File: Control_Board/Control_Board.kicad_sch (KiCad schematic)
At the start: 56 parts, among them J1 DE9_Receptacle, J2 DE9_Receptacle, J3 Conn_01x04, J4 GPS_ANT, J5 Conn_01x02, SW2 SW_SPST, U1 STM32F446RCTx, U3 SN65HVD256D, U6 AP2204K-ADJ, U7 AP2204K-ADJ, U8 SN65HVD256D, U9 NEO-XM, Y3 8M, Y4 32.768k

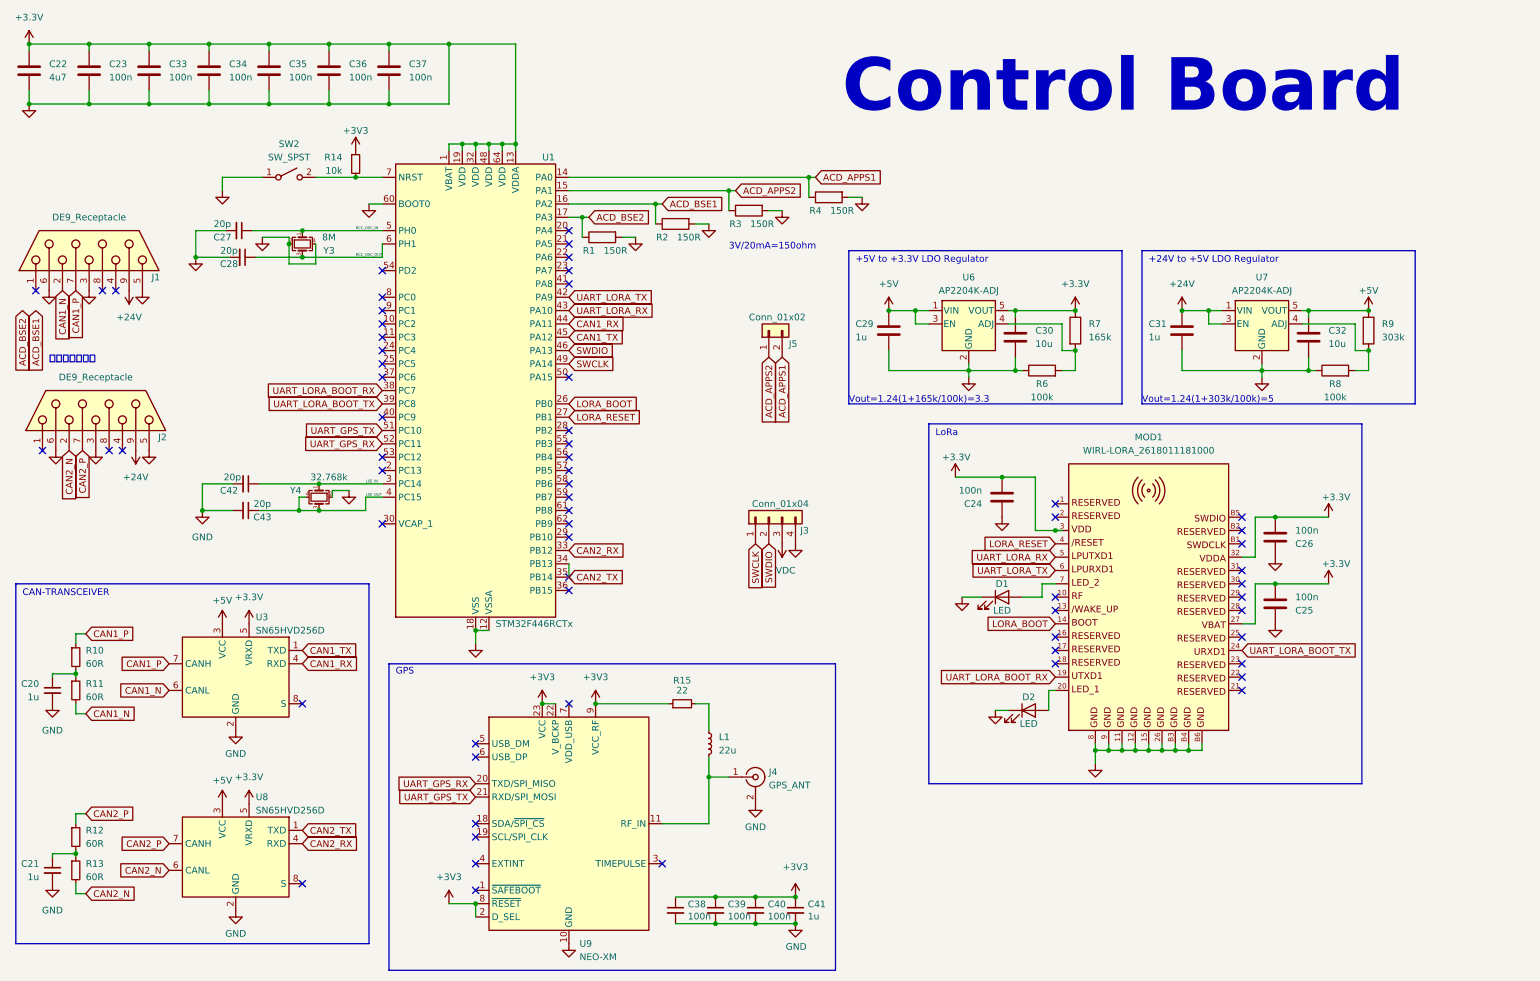
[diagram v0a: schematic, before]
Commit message: fix: power symbol and connector
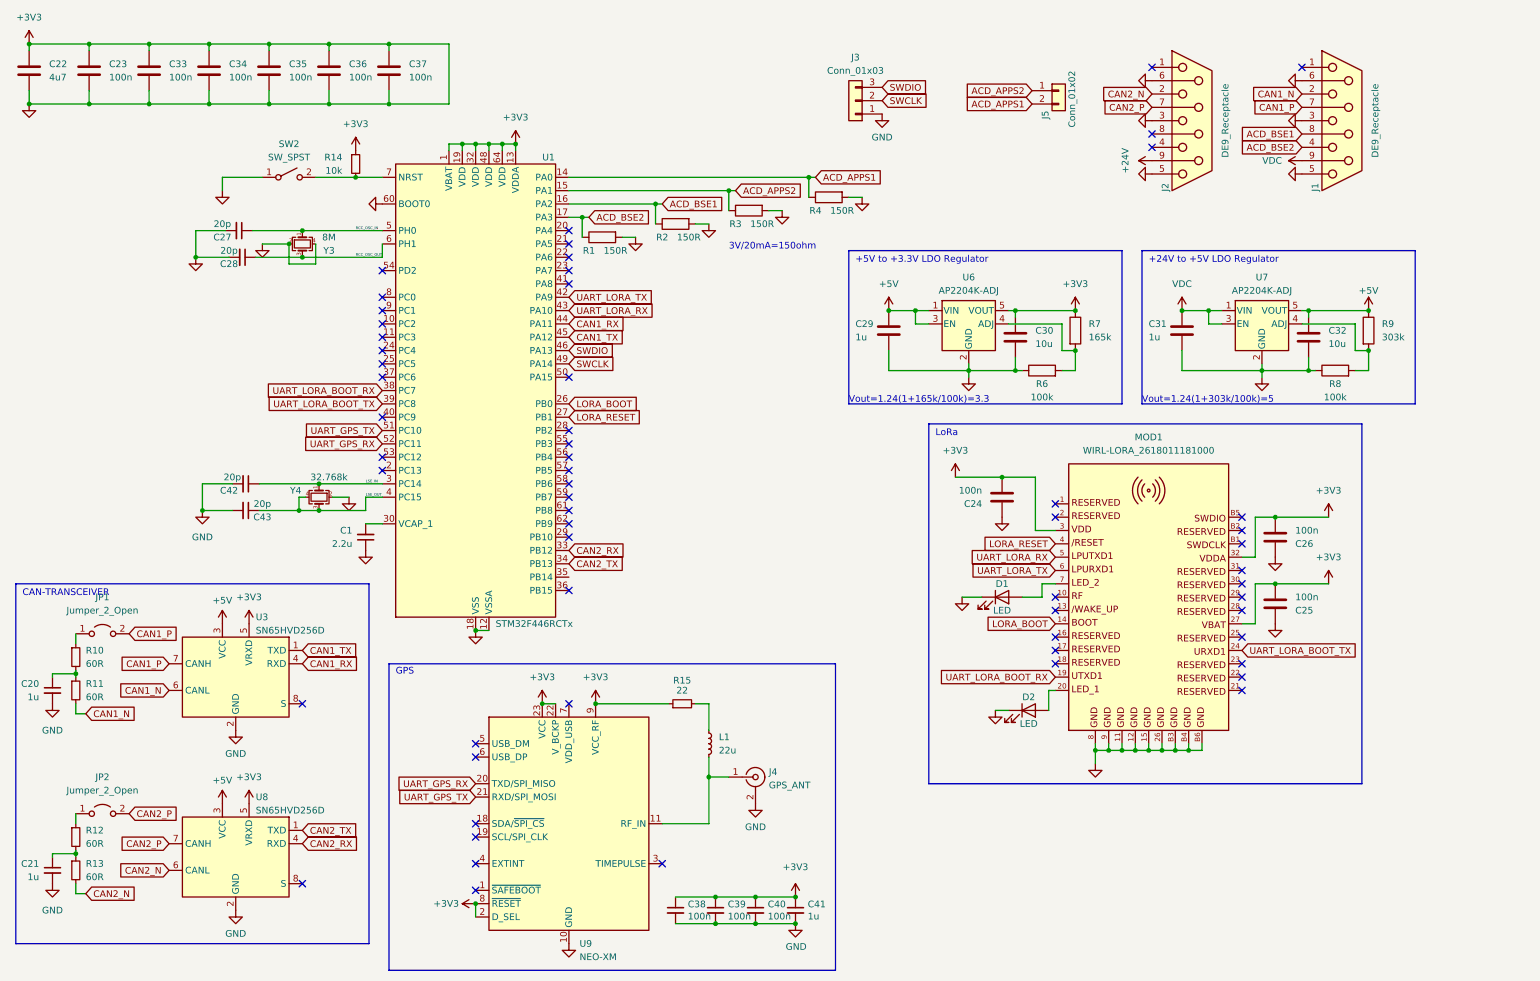
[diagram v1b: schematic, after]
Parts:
- removed J3: Conn_01x04, symbol Connector_Generic:Conn_01x04
- added C1: 2.2u, symbol Device:C_Small
- added J3: Conn_01x03, symbol Connector_Generic:Conn_01x03
- added JP1, JP2: Jumper_2_Open, symbol Jumper:Jumper_2_Open
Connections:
- net +3.3V is gone; now on net +3V3: C20.2, C21.2, C22.1, C22.2, C23.1, C23.2, C24.1, C24.2, C25.1, C25.2, C26.1, C26.2, C27.2, C28.2, C29.2, C30.1, C30.2, C31.2, C32.2, C33.1, C33.2, C34.1, C34.2, C35.1, C35.2, C36.1, C36.2, C37.1, C37.2, C38.2, C39.2, C40.2, C41.2, C42.2, C43.2, D1.1 (K), D2.1 (K), J1.3, J1.5, J1.6, J2.3, J2.5, J2.6, J4.2 (Ext), MOD1.11, MOD1.12, MOD1.15, MOD1.26, MOD1.27, MOD1.3, MOD1.32, MOD1.8, MOD1.9, MOD1.B3, MOD1.B4, MOD1.B6, R1.2, R2.2, R3.2, R4.2, R6.1, R7.1, R8.1, SW2.1 (A), U1.1 (VBAT), U1.12 (VSSA), U1.13 (VDDA), U1.18 (VSS), U1.19 (VDD), U1.31 (VSS), U1.32 (VDD), U1.47 (VSS), U1.48 (VDD), U1.60 (BOOT0), U1.63 (VSS), U1.64 (VDD), U3.2 (GND), U3.5 (VRXD), U6.2 (GND), U6.5 (VOUT), U7.2 (GND), U8.2 (GND), U8.5 (VRXD), U9.10 (GND), U9.12 (GND), U9.13 (GND), U9.24 (GND), Y3.2, Y3.4, Y4.2
- net +24V: no longer C31.1, J1.9, U7.1 (VIN), U7.3 (EN)
- net +3V3: now also C1.1, J3.1 (Pin_1)
- net ACD_BSE1: now also J1.8
- net ACD_BSE2: now also J1.4
- net CAN1_P: now also JP1.2 (B); no longer R10.1
- net CAN2_P: now also JP2.2 (B); no longer R12.1
- net CAN2_TX: no longer U1.35 (PB14)
- net SWCLK: now also J3.2 (Pin_2)
- net SWDIO: now also J3.3 (Pin_3)
- net VDC: now also C31.1, J1.9, U7.1 (VIN), U7.3 (EN)
- net at U1.30 (VCAP_1): now also C1.2
- new net: JP1.1 (A), R10.1
- new net: JP2.1 (A), R12.1
- no-connect marks 63 -> 59
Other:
- note removed: "Control Board"
- note removed: "還不確定要接哪"
- moved on the sheet: J1, J2, J5

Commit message: feat: implement schematic and select footprints
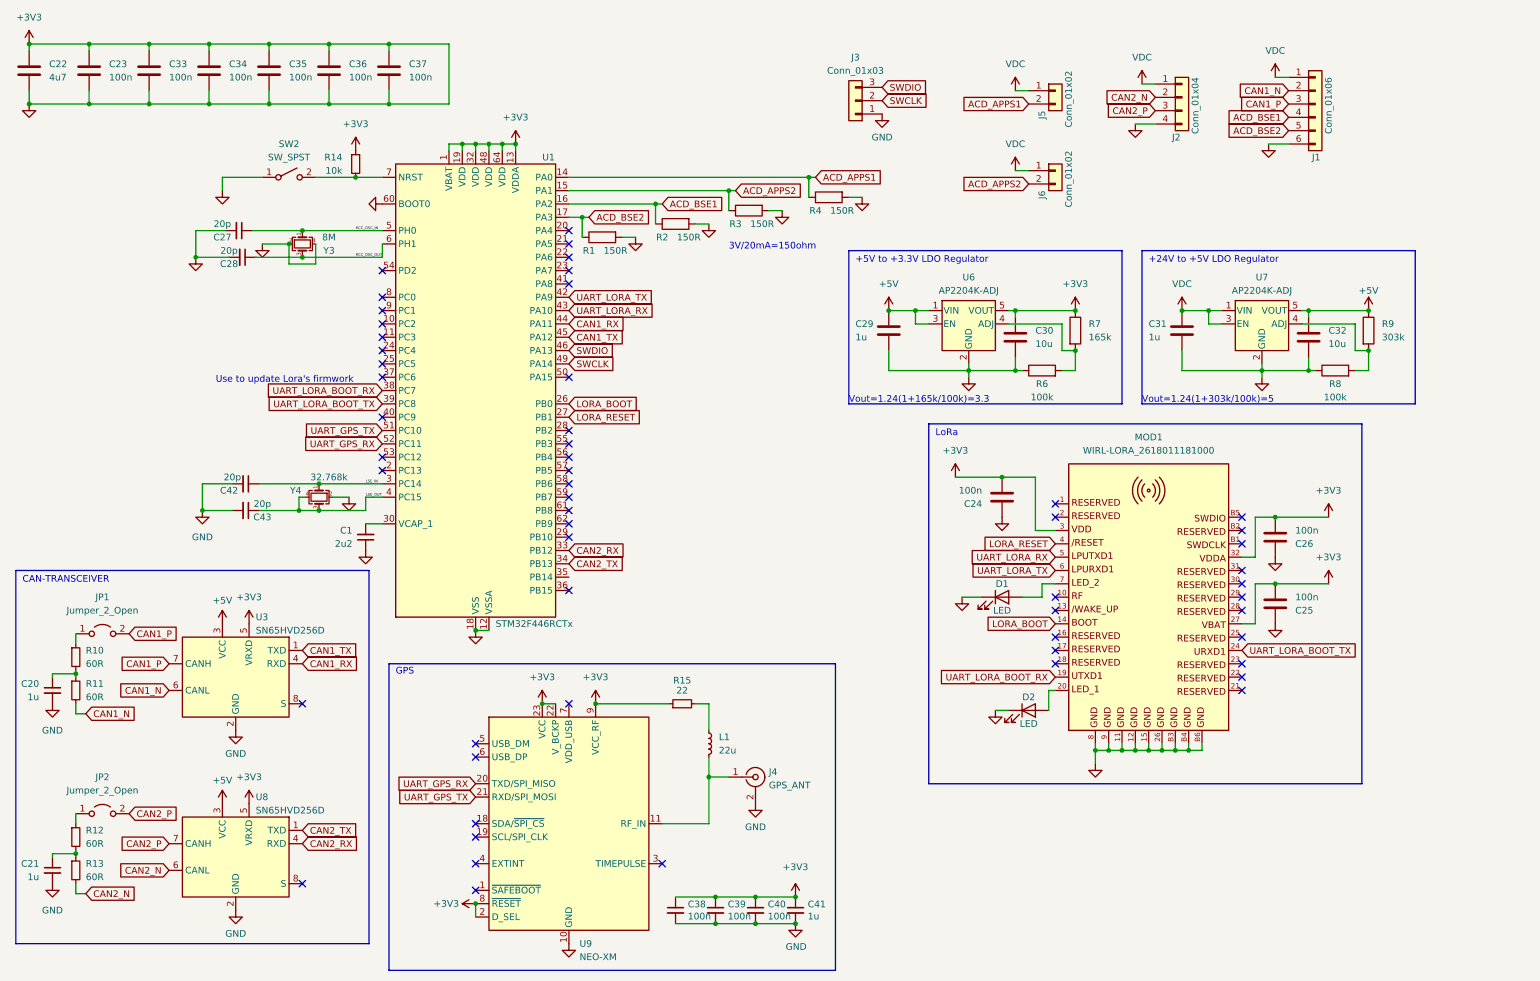
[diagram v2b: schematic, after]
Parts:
- removed J1, J2: DE9_Receptacle, symbol Connector:DE9_Receptacle
- added J1: Conn_01x06, Connector_JST:JST_XH_B6B-XH-A_1x06_P2.50mm_Vertical, symbol Connector_Generic:Conn_01x06
- added J2: Conn_01x04, Connector_JST:JST_XH_B4B-XH-A_1x04_P2.50mm_Vertical, symbol Connector_Generic:Conn_01x04
- added J6: Conn_01x02, Connector_JST:JST_XH_B2B-XH-A_1x02_P2.50mm_Vertical, symbol Connector_Generic:Conn_01x02
- C1: value 2.2u -> 2u2; footprint (none) -> Capacitor_SMD:C_0805_2012Metric
- C22: footprint Resistor_SMD:R_0603_1608Metric -> Capacitor_SMD:C_0805_2012Metric
- D1, D2: footprint (none) -> LED_SMD:LED_0805_2012Metric
- J3: footprint (none) -> Connector_PinHeader_2.54mm:PinHeader_1x03_P2.54mm_Vertical
- J5: footprint (none) -> Connector_JST:JST_XH_B2B-XH-A_1x02_P2.50mm_Vertical
- JP1, JP2: footprint (none) -> PCM_Jumper_AKL:Jumper_P2.54mm_D0.7mm
- R1, R2, R3, R4: footprint (none) -> Resistor_SMD:R_0603_1608Metric
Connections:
- net +3V3: now also J1.6 (Pin_6), J2.4 (Pin_4)
- net ACD_APPS2: now also J6.2 (Pin_2); no longer J5.1 (Pin_1)
- net ACD_BSE1: now also J1.4 (Pin_4)
- net ACD_BSE2: now also J1.5 (Pin_5)
- net CAN1_N: now also J1.2 (Pin_2)
- net CAN1_P: now also J1.3 (Pin_3)
- net CAN2_N: now also J2.2 (Pin_2)
- net CAN2_P: now also J2.3 (Pin_3)
- net VDC: now also J5.1 (Pin_1), J1.1 (Pin_1), J2.1 (Pin_1), J6.1 (Pin_1)
- no-connect marks 59 -> 55
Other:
- note added: "Use to update Lora's firmwork"
- moved on the sheet: J5

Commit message: fix(ctrl_board): correct 100nF cap footprint
100nF capacitor footprint should be 0603 but using 0402 originally.
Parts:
- C23, C24, C25, C26, C33, C34, C35, C36, C37: footprint Capacitor_SMD:C_0402_1005Metric -> Capacitor_SMD:C_0603_1608Metric
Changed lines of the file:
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@@
       (effects (font (size 1.27 1.27)) (justify left))
     )
-    (property "Footprint" "Capacitor_SMD:C_0402_1005Metric" (at 31.4452 29.21 0)
+    (property "Footprint" "Capacitor_SMD:C_0603_1608Metric" (at 31.4452 29.21 0)
       (effects (font (size 1.27 1.27)) hide)
     )
@@
       (effects (font (size 1.27 1.27)) (justify left))
     )
-    (property "Footprint" "Capacitor_SMD:C_0402_1005Metric" (at 65.7352 29.21 0)
+    (property "Footprint" "Capacitor_SMD:C_0603_1608Metric" (at 65.7352 29.21 0)
       (effects (font (size 1.27 1.27)) hide)
     )
@@
       (effects (font (size 1.27 1.27)) (justify left))
     )
-    (property "Footprint" "Capacitor_SMD:C_0402_1005Metric" (at 257.5052 123.19 0)
+    (property "Footprint" "Capacitor_SMD:C_0603_1608Metric" (at 257.5052 123.19 0)
       (effects (font (size 1.27 1.27)) hide)
     )
@@
       (effects (font (size 1.27 1.27)) (justify left))
     )
-    (property "Footprint" "Capacitor_SMD:C_0402_1005Metric" (at 77.1652 29.21 0)
+    (property "Footprint" "Capacitor_SMD:C_0603_1608Metric" (at 77.1652 29.21 0)
       (effects (font (size 1.27 1.27)) hide)
     )
@@
       (effects (font (size 1.27 1.27)) (justify left))
     )
-    (property "Footprint" "Capacitor_SMD:C_0402_1005Metric" (at 54.3052 29.21 0)
+    (property "Footprint" "Capacitor_SMD:C_0603_1608Metric" (at 54.3052 29.21 0)
       (effects (font (size 1.27 1.27)) hide)
     )
@@
       (effects (font (size 1.27 1.27)) (justify left))
     )
-    (property "Footprint" "Capacitor_SMD:C_0402_1005Metric" (at 42.8752 29.21 0)
+    (property "Footprint" "Capacitor_SMD:C_0603_1608Metric" (at 42.8752 29.21 0)
       (effects (font (size 1.27 1.27)) hide)
     )
@@
       (effects (font (size 1.27 1.27)) (justify left))
     )
-    (property "Footprint" "Capacitor_SMD:C_0402_1005Metric" (at 203.5048 102.87 0)
+    (property "Footprint" "Capacitor_SMD:C_0603_1608Metric" (at 203.5048 102.87 0)
       (effects (font (size 1.27 1.27)) hide)
     )
@@
       (effects (font (size 1.27 1.27)) (justify left))
     )
-    (property "Footprint" "Capacitor_SMD:C_0402_1005Metric" (at 88.5952 29.21 0)
+    (property "Footprint" "Capacitor_SMD:C_0603_1608Metric" (at 88.5952 29.21 0)
       (effects (font (size 1.27 1.27)) hide)
     )
@@
       (effects (font (size 1.27 1.27)) (justify left))
     )
-    (property "Footprint" "Capacitor_SMD:C_0402_1005Metric" (at 257.5052 110.49 0)
-      (effects (font (size 1.27 1.27)) hide)
-    )
+    (property "Footprint" "Capacitor_SMD:C_0603_1608Metric" (at 257.5052 110.49 0)
+      (effects (font (size 1.27 1.27)) hide)
+    )

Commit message: feat: implement control board layout
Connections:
- net +3V3: no longer C1.1, C20.2, C21.2, C22.2, C23.2, C24.1, C25.1, C26.1, C27.2, C28.2, C29.2, C30.2, C31.2, C32.2, C33.2, C34.2, C35.2, C36.2, C37.2, C38.2, C39.2, C40.2, C41.2, C42.2, C43.2, D1.1 (K), D2.1 (K), J1.6 (Pin_6), J2.4 (Pin_4), J3.1 (Pin_1), J4.2 (Ext), MOD1.11, MOD1.12, MOD1.15, MOD1.26, MOD1.8, MOD1.9, MOD1.B3, MOD1.B4, MOD1.B6, R1.2, R2.2, R3.2, R4.2, R6.1, R8.1, SW2.1 (A), U1.12 (VSSA), U1.18 (VSS), U1.31 (VSS), U1.47 (VSS), U1.60 (BOOT0), U1.63 (VSS), U3.2 (GND), U6.2 (GND), U7.2 (GND), U8.2 (GND), U9.10 (GND), U9.12 (GND), U9.13 (GND), U9.24 (GND), Y3.2, Y3.4, Y4.2
- new net GND: C1.1, C20.2, C21.2, C22.2, C23.2, C24.1, C25.1, C26.1, C27.2, C28.2, C29.2, C30.2, C31.2, C32.2, C33.2, C34.2, C35.2, C36.2, C37.2, C38.2, C39.2, C40.2, C41.2, C42.2, C43.2, D1.1 (K), D2.1 (K), J1.6 (Pin_6), J2.4 (Pin_4), J3.1 (Pin_1), J4.2 (Ext), MOD1.11, MOD1.12, MOD1.15, MOD1.26, MOD1.8, MOD1.9, MOD1.B3, MOD1.B4, MOD1.B6, R1.2, R2.2, R3.2, R4.2, R6.1, R8.1, SW2.1 (A), U1.12 (VSSA), U1.18 (VSS), U1.31 (VSS), U1.47 (VSS), U1.60 (BOOT0), U1.63 (VSS), U3.2 (GND), U6.2 (GND), U7.2 (GND), U8.2 (GND), U9.10 (GND), U9.12 (GND), U9.13 (GND), U9.24 (GND), Y3.2, Y3.4, Y4.2
- no-connect marks 55 -> 56
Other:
- note added: "Jumper to toggle CAN termination."
- note added: "connect to DB9"
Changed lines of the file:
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@@
   (junction (at 187.96 71.12) (diameter 0) (color 0 0 0 0)
   )
+  (junction (at 99.06 39.37) (diameter 0) (color 0 0 0 0)
+  )
   (junction (at 116.84 146.05) (diameter 0) (color 0 0 0 0)
   )
@@
   (junction (at 218.44 78.74) (diameter 0) (color 0 0 0 0)
   )
-  (junction (at 111.76 39.37) (diameter 0) (color 0 0 0 0)
-  )
   (junction (at 138.43 50.8) (diameter 0) (color 0 0 0 0)
   )
@@
   (junction (at 256.54 123.19) (diameter 0) (color 0 0 0 0)
   )
-  (junction (at 87.63 31.75) (diameter 0) (color 0 0 0 0)
-  )
   (junction (at 207.01 82.55) (diameter 0) (color 0 0 0 0)
   )
@@
   (no_connect (at 250.19 125.73))
   (no_connect (at 86.36 63.5))
+  (no_connect (at 121.92 121.92))
   (no_connect (at 214.63 138.43))
   (no_connect (at 86.36 73.66))
@@
     (stroke (width 0) (type default))
   )
+  (wire (pts (xy 99.06 20.32) (xy 99.06 39.37))
+    (stroke (width 0) (type default))
+  )
   (wire (pts (xy 218.44 78.74) (xy 218.44 82.55))
     (stroke (width 0) (type default))
@@
     (stroke (width 0) (type default))
   )
-  (wire (pts (xy 87.63 31.75) (xy 99.06 31.75))
-    (stroke (width 0) (type default))
-  )
   (wire (pts (xy 41.91 20.32) (xy 30.48 20.32))
     (stroke (width 0) (type default))
@@
     (stroke (width 0) (type default))
   )
-  (wire (pts (xy 99.06 20.32) (xy 99.06 31.75))
-    (stroke (width 0) (type default))
-  )
   (wire (pts (xy 50.8 60.96) (xy 50.8 55.88))
     (stroke (width 0) (type default))
@@
     (effects (font (size 1.27 1.27)) (justify left bottom))
   )
+  (text "connect to DB9" (at 226.06 40.64 0)
+    (effects (font (size 1.27 1.27)) (justify left bottom))
+  )
+  (text "Jumper to toggle CAN termination." (at 17.78 157.48 0)
+    (effects (font (size 1.27 1.27)) (justify left bottom))
+  )
   (text "CAN-TRANSCEIVER" (at 17.78 123.19 0)
     (effects (font (size 1.27 1.27)) (justify left bottom))
@@
     (effects (font (size 1.27 1.27)) (justify left bottom))
   )
+  (text "connect to DB9" (at 251.46 44.45 0)
+    (effects (font (size 1.27 1.27)) (justify left bottom))
+  )
   (label "LSE_OUT" (at 83.185 106.68 0) (fields_autoplaced)
     (effects (font (size 0.5 0.5)) (justify left bottom))
@@
     )
   )
-  (symbol (lib_id "power:+3V3") (at 111.76 39.37 0) (unit 1)
-    (in_bom yes) (on_board yes) (dnp no) (fields_autoplaced)
-    (property "Reference" "#PWR041" (at 111.76 43.18 0)
-      (effects (font (size 1.27 1.27)) hide)
-    )
-    (property "Value" "+3V3" (at 111.76 34.29 0)
-      (effects (font (size 1.27 1.27)))
-    )
-    (property "Footprint" "" (at 111.76 39.37 0)
-      (effects (font (size 1.27 1.27)) hide)
-    )
-    (property "Datasheet" "" (at 111.76 39.37 0)
-      (effects (font (size 1.27 1.27)) hide)
-    )
-    (pin "1")
-    (instances
-      (project "Control_Board"
-        (path "/0d995863-6cec-4b88-9697-48659a6a1176"
-          (reference "#PWR041") (unit 1)
-        )
-      )
-    )
-  )
   (symbol (lib_id "power:VDC") (at 256.54 26.67 0) (mirror y) (unit 1)
     (in_bom yes) (on_board yes) (dnp no)
@@
   (symbol (lib_id "Connector_Generic:Conn_01x04") (at 238.76 30.48 0) (unit 1)
     (in_bom yes) (on_board yes) (dnp no)
-    (property "Reference" "J2" (at 236.855 38.1 0)
+    (property "Reference" "J2" (at 237.49 25.4 0)
       (effects (font (size 1.27 1.27)) (justify left))
     )
@@
   (symbol (lib_id "Connector_Generic:Conn_01x06") (at 264.16 31.75 0) (unit 1)
     (in_bom yes) (on_board yes) (dnp no)
-    (property "Reference" "J1" (at 263.525 41.91 0)
+    (property "Reference" "J1" (at 264.16 24.13 0)
       (effects (font (size 1.27 1.27)) (justify left))
     )
